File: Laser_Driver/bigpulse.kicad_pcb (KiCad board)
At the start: 2 copper layers, 111.8 x 35.6 mm, 63 parts, among them IC1 UCC27424P, J1 TRIG, J2 12VIN, J3 BANANA_V+, J4 BANANA_V-, Q1 ZTX415, Q2 ZTX415, Q3 ZTX415, Q4 ZTX415, Q5 STP45N65M5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

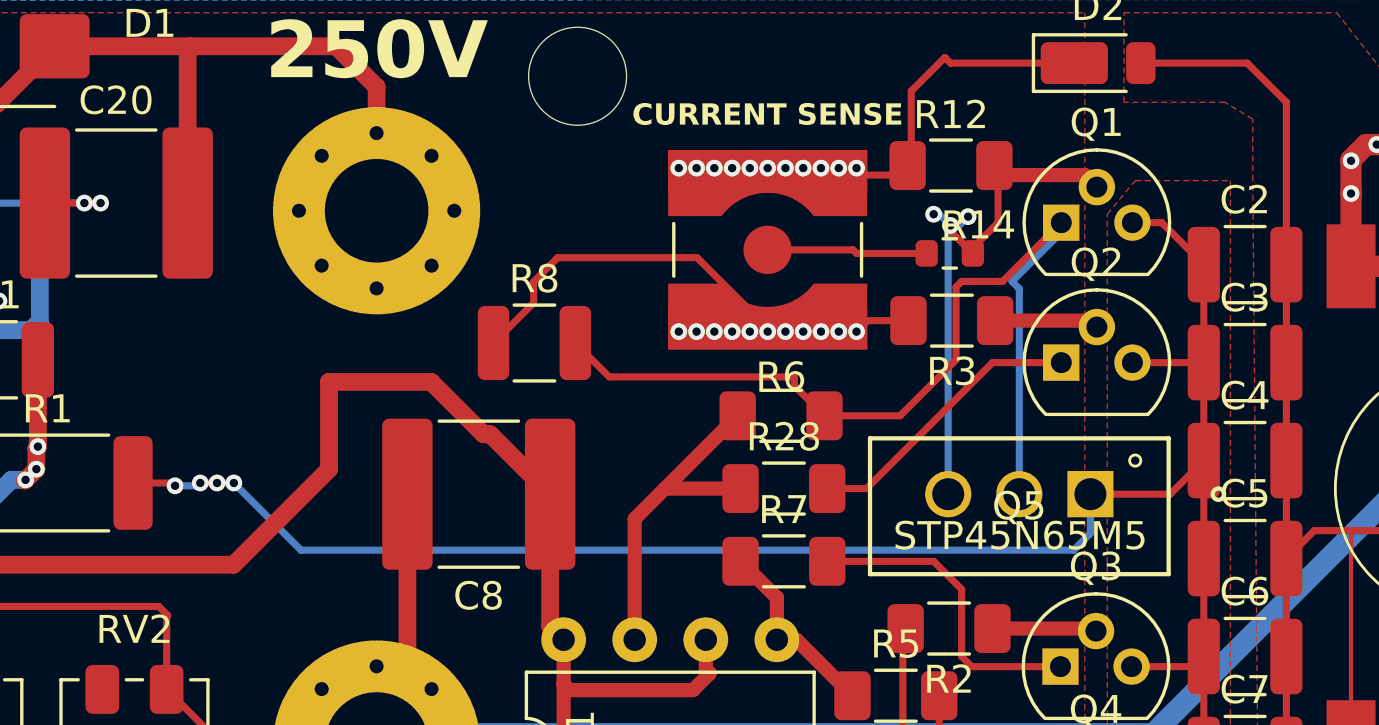
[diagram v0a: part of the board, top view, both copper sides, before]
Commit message: Minor improvements after prototyping
Legs of MOSFET were switched.
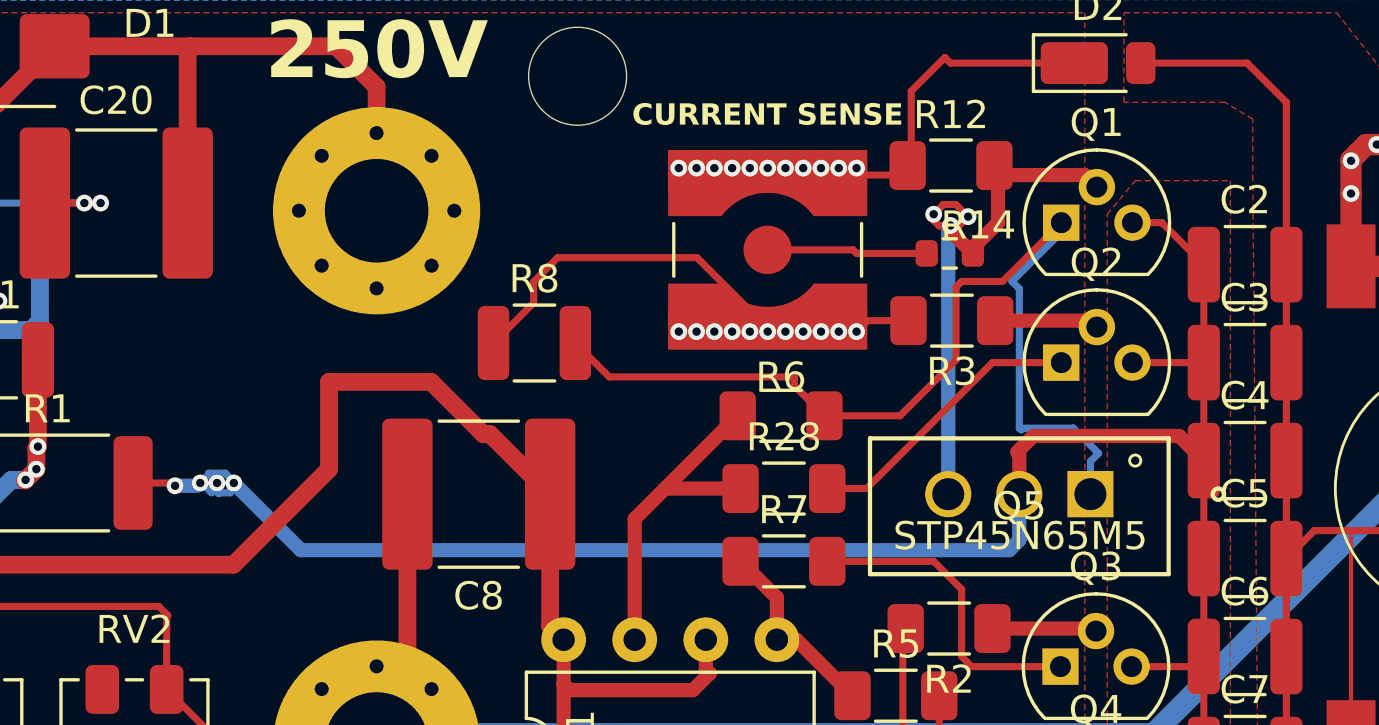
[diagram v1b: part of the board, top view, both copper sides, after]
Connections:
- Q5 pad 1: Net-(Q1-C) -> TRIG1
- Q5 pad 2: TRIG1 -> Net-(Q1-C)
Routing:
- net Net-(Q1-C): track 71.0 -> 76.0 mm
- net TRIG1: track 33.5 -> 36.1 mm
- net Net-(Q1-E): track 19.5 -> 21.2 mm
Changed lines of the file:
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@@
 			(layers "*.Cu" "*.Mask")
 			(remove_unused_layers no)
-			(net 1 "Net-(Q1-C)")
-			(pinfunction "D")
-			(pintype "passive")
+			(net 6 "TRIG1")
+			(pinfunction "G")
+			(pintype "input")
 		)
 		(pad "2" thru_hole circle
@@
 			(layers "*.Cu" "*.Mask")
 			(remove_unused_layers no)
-			(net 6 "TRIG1")
-			(pinfunction "G")
-			(pintype "input")
+			(net 1 "Net-(Q1-C)")
+			(pinfunction "D")
+			(pintype "passive")
 		)
 		(pad "3" thru_hole circle
@@
 		)
 		(embedded_fonts no)
+		(model "${KIPRJMOD}/NUBB-45.STEP"
+			(offset
+				(xyz 0 2.25 0)
+			)
+			(scale
+				(xyz 1 1 1)
+			)
+			(rotate
+				(xyz -0 -0 -0)
+			)
+		)
 	)
 	(footprint "Resistor_SMD:R_1210_3225Metric"
@@
 	)
 	(segment
+		(start 220.05 101)
+		(end 219.17 100.12)
+		(width 0.508)
+		(layer "F.Cu")
+		(net 1)
+	)
+	(segment
 		(start 217.47 108.36)
 		(end 219.69 108.36)
@@
 	)
 	(segment
-		(start 219.69 108.36)
-		(end 220.05 108)
-		(width 0.254)
+		(start 213.46 100.78)
+		(end 213.46 102.2)
+		(width 0.508)
 		(layer "F.Cu")
 		(net 1)
 	)
 	(segment
-		(start 218.85 102.2)
-		(end 220.05 101)
+		(start 219.69 108.36)
+		(end 220.05 108)
 		(width 0.254)
 		(layer "F.Cu")
@@
 	)
 	(segment
-		(start 217.5 97.5)
-		(end 220.05 97.5)
-		(width 0.254)
+		(start 213.96 100.12)
+		(end 213.38 100.7)
+		(width 0.508)
 		(layer "F.Cu")
 		(net 1)
 	)
 	(segment
-		(start 216 102.2)
-		(end 218.85 102.2)
+		(start 217.5 97.5)
+		(end 220.05 97.5)
 		(width 0.254)
 		(layer "F.Cu")
@@
 	)
 	(segment
-		(start 184.8 101.8)
-		(end 185.4 101.8)
-		(width 0.254)
-		(layer "F.Cu")
-		(net 1)
-	)
-	(segment
 		(start 181.8 101.8)
 		(end 183.2 101.8)
@@
 	)
 	(segment
+		(start 213.38 100.7)
+		(end 213.46 100.78)
+		(width 0.254)
+		(layer "F.Cu")
+		(net 1)
+	)
+	(segment
 		(start 219.44 111.5)
 		(end 220.05 111.5)
@@
 	)
 	(segment
+		(start 219.17 100.12)
+		(end 213.96 100.12)
+		(width 0.508)
+		(layer "F.Cu")
+		(net 1)
+	)
+	(segment
 		(start 184.2 101.8)
 		(end 184.8 101.8)
@@
 	)
 	(segment
+		(start 185.4 101.76)
+		(end 185.4 101.8)
+		(width 0.254)
+		(layer "B.Cu")
+		(net 1)
+	)
+	(segment
+		(start 213.1 104.2)
+		(end 187.8 104.2)
+		(width 0.508)
+		(layer "B.Cu")
+		(net 1)
+	)
+	(segment
+		(start 184.89 102.15)
+		(end 185.27 102.15)
+		(width 0.254)
+		(layer "B.Cu")
+		(net 1)
+	)
+	(segment
+		(start 184.8 102.12)
+		(end 184.86 102.18)
+		(width 0.254)
+		(layer "B.Cu")
+		(net 1)
+	)
+	(segment
+		(start 184.2 101.8)
+		(end 184.5 101.5)
+		(width 0.254)
+		(layer "B.Cu")
+		(net 1)
+	)
+	(segment
 		(start 184.1 101.9)
 		(end 184.2 101.8)
@@
 	)
 	(segment
-		(start 216 102.2)
-		(end 216 103.6)
+		(start 213.46 102.2)
+		(end 213.46 103.84)
+		(width 0.508)
+		(layer "B.Cu")
+		(net 1)
+	)
+	(segment
+		(start 185.27 102.15)
+		(end 185.27 101.93)
 		(width 0.254)
 		(layer "B.Cu")
@@
 	)
 	(segment
-		(start 215.4 104.2)
-		(end 187.8 104.2)
+		(start 213.46 103.84)
+		(end 213.1 104.2)
+		(width 0.508)
+		(layer "B.Cu")
+		(net 1)
+	)
+	(segment
+		(start 184.5 101.5)
+		(end 184.5 101.45)
+		(width 0.254)
+		(layer "B.Cu")
+		(net 1)
+	)
+	(segment
+		(start 184.8 101.8)
+		(end 184.8 101.95)
+		(width 0.254)
+		(layer "B.Cu")
+		(net 1)
+	)
+	(segment
+		(start 184.8 101.95)
+		(end 184.6 102.15)
+		(width 0.254)
+		(layer "B.Cu")
+		(net 1)
+	)
+	(segment
+		(start 185.09 101.45)
+		(end 185.4 101.76)
+		(width 0.254)
+		(layer "B.Cu")
+		(net 1)
+	)
+	(segment
+		(start 184.6 102.15)
+		(end 184.35 101.9)
+		(width 0.254)
+		(layer "B.Cu")
+		(net 1)
+	)
+	(segment
+		(start 184.35 101.9)
+		(end 184.1 101.9)
 		(width 0.254)
 		(layer "B.Cu")
@@
 		(start 187.8 104.2)
 		(end 185.4 101.8)
+		(width 0.508)
+		(layer "B.Cu")
+		(net 1)
+	)
+	(segment
+		(start 184.8 101.8)
+		(end 184.8 102.12)
+		(width 0.254)
+		(layer "B.Cu")
+		(net 1)
+	)
+	(segment
+		(start 184.86 102.18)
+		(end 184.89 102.15)
 		(width 0.254)
 		(layer "B.Cu")
@@
 	)
 	(segment
-		(start 216 103.6)
-		(end 215.4 104.2)
+		(start 185.27 101.93)
+		(end 185.4 101.8)
 		(width 0.254)
 		(layer "B.Cu")
@@
 		(start 183.3 101.9)
 		(end 184.1 101.9)
+		(width 0.508)
+		(layer "B.Cu")
+		(net 1)
+	)
+	(segment
+		(start 184.5 101.45)
+		(end 185.09 101.45)
 		(width 0.254)
 		(layer "B.Cu")
@@
 	)
 	(segment
+		(start 210.6 92.62)
+		(end 210.62 92.6)
+		(width 0.254)
+		(layer "F.Cu")
+		(net 3)
+	)
+	(segment
 		(start 211 92.6)
 		(end 211 92.8)
@@
 	)
 	(segment
+		(start 210.4 92.42)
+		(end 210.6 92.62)
+		(width 0.254)
+		(layer "F.Cu")
+		(net 3)
+	)
+	(segment
+		(start 211.314839 92.6)
+		(end 211.629679 92.28516)
+		(width 0.254)
+		(layer "F.Cu")
+		(net 3)
+	)
+	(segment
+		(start 211.194519 91.85)
+		(end 211.629679 92.28516)
+		(width 0.254)
+		(layer "F.Cu")
+		(net 3)
+	)
+	(segment
 		(start 215.8 90.8)
 		(end 216.23 91.23)
@@
 	)
 	(segment
+		(start 210.75 91.85)
+		(end 211.194519 91.85)
+		(width 0.254)
+		(layer "F.Cu")
+		(net 3)
+	)
+	(segment
+		(start 211 92.6)
+		(end 211.314839 92.6)
+		(width 0.254)
+		(layer "F.Cu")
+		(net 3)
+	)
+	(segment
 		(start 212.7 90.8)
 		(end 215.8 90.8)
@@
 		(start 211.8 93.4)
 		(end 212.7 92.5)
+		(width 0.508)
+		(layer "F.Cu")
+		(net 3)
+	)
+	(segment
+		(start 210.4 92.2)
+		(end 210.75 91.85)
+		(width 0.254)
+		(layer "F.Cu")
+		(net 3)
+	)
+	(segment
+		(start 210.62 92.6)
+		(end 211 92.6)
 		(width 0.254)
 		(layer "F.Cu")
@@
 		(start 212.7 92.5)
 		(end 212.7 90.8)
+		(width 0.508)
+		(layer "F.Cu")
+		(net 3)
+	)
+	(segment
+		(start 210.4 92.2)
+		(end 210.4 92.42)
 		(width 0.254)
 		(layer "F.Cu")
@@
 		(start 211 92.8)
 		(end 211.8 93.6)
-		(width 0.254)
+		(width 0.508)
 		(layer "F.Cu")
 		(net 3)
@@
 		(start 210.92 102.2)
 		(end 210.92 92.68)
-		(width 0.254)
-		(layer "B.Cu")
-		(net 3)
-	)
-	(segment
-		(start 211.314839 92.6)
-		(end 211.629679 92.28516)
-		(width 0.254)
-		(layer "B.Cu")
-		(net 3)
-	)
-	(segment
-		(start 210.6 92.2)
-		(end 211 92.6)
-		(width 0.254)
-		(layer "B.Cu")
-		(net 3)
-	)
-	(segment
-		(start 210.4 92.2)
-		(end 210.6 92.2)
-		(width 0.254)
-		(layer "B.Cu")
-		(net 3)
-	)
-	(segment
-		(start 211 92.6)
-		(end 211.314839 92.6)
-		(width 0.254)
+		(width 0.508)
 		(layer "B.Cu")
 		(net 3)
@@
 	)
 	(segment
+		(start 213.46 94.86)
+		(end 213.46 99.84)
+		(width 0.254)
+		(layer "B.Cu")
+		(net 6)
+	)
+	(segment
 		(start 214.96 92.84)
 		(end 213.2 94.6)
@@
 	)
 	(segment
+		(start 215.39 99.84)
+		(end 216.29 100.74)
+		(width 0.254)
+		(layer "B.Cu")
+		(net 6)
+	)
+	(segment
+		(start 213.46 99.84)
+		(end 213.53 99.91)
+		(width 0.254)
+		(layer "B.Cu")
+		(net 6)
+	)
+	(segment
+		(start 216.29 100.74)
+		(end 216 101.03)
+		(width 0.254)
+		(layer "B.Cu")
+		(net 6)
+	)
+	(segment
 		(start 213.2 94.6)
 		(end 213.46 94.86)
@@
 	)
 	(segment
-		(start 213.46 94.86)
-		(end 213.46 102.2)
+		(start 216 101.03)
+		(end 216 102.2)
+		(width 0.254)
+		(layer "B.Cu")
+		(net 6)
+	)
+	(segment
+		(start 213.46 99.84)
+		(end 215.39 99.84)
 		(width 0.254)
 		(layer "B.Cu")
